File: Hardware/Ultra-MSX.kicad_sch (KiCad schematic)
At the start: 9 parts

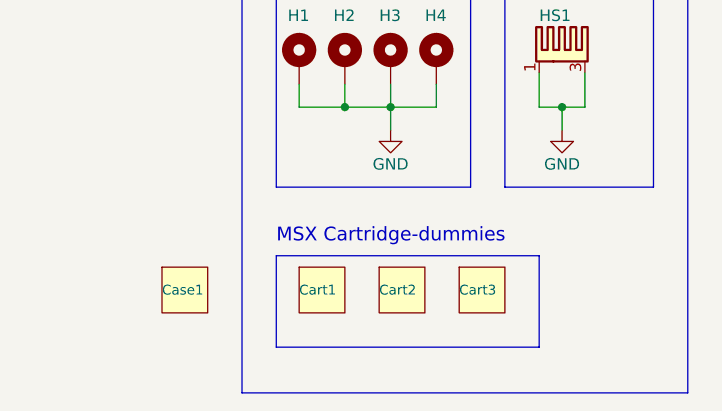
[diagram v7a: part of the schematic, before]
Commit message: Redesigning of the IO-shield, to make room for Keyboard, power and USB.
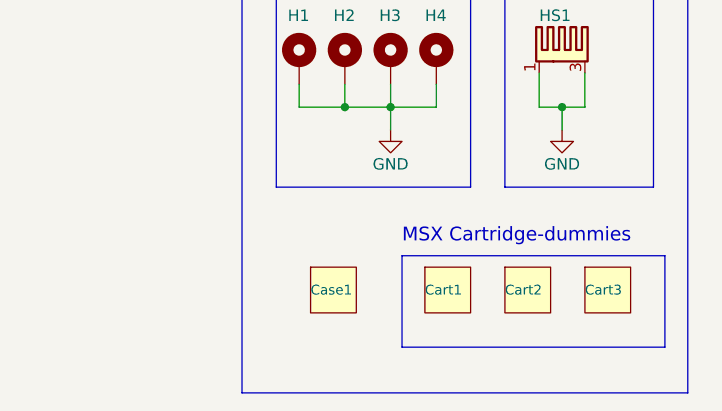
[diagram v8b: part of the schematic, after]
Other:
- moved on the sheet: Cart1, Cart2, Cart3, Case1
